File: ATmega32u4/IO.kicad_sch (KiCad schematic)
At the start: 14 parts, among them SW1 HWB, SW2 RESET

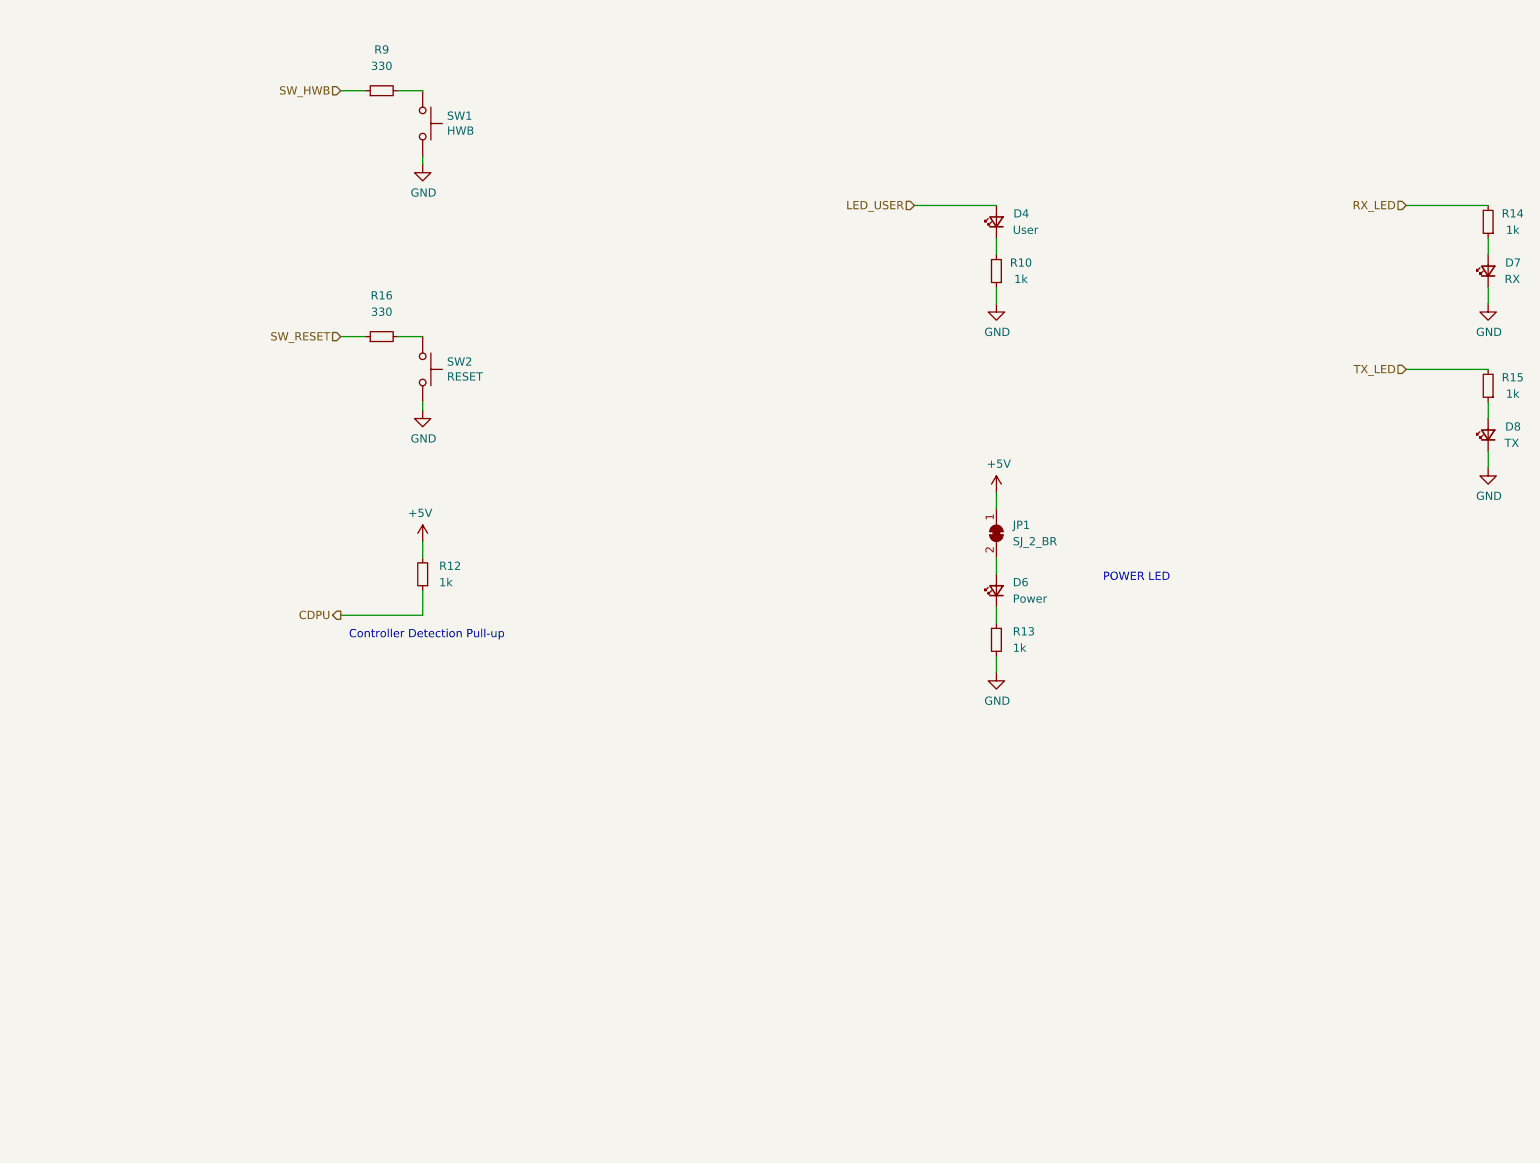
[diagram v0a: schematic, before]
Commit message: Schematic, routing and layout changes post review.
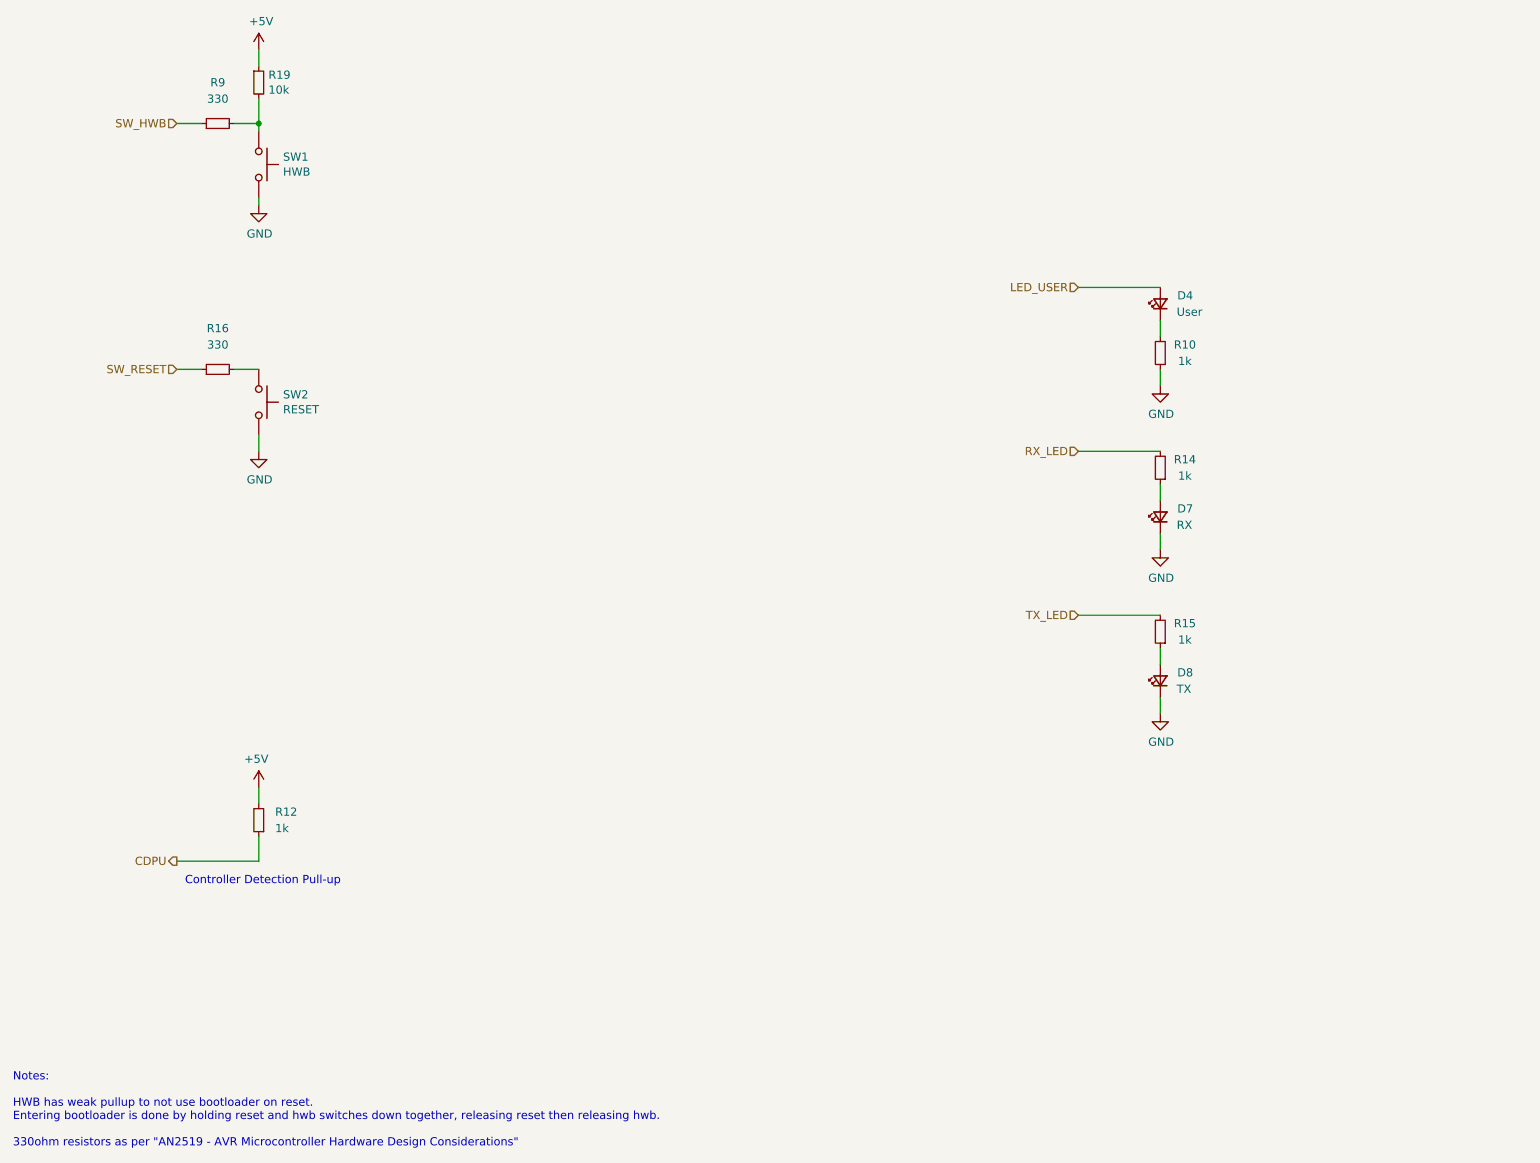
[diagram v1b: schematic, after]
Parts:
- removed D6: Power, LED_SMD:LED_0603_1608Metric, symbol Device:LED_Small
- removed JP1: SJ_2_BR, Jumper:SolderJumper-2_P1.3mm_Bridged_RoundedPad1.0x1.5mm, symbol Jumper:SolderJumper_2_Bridged
- removed R13: 1k, Resistor_SMD:R_0603_1608Metric, symbol Device:R_Small
- added R19: 10k, Resistor_SMD:R_0603_1608Metric, symbol Device:R_Small
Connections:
- net +5V: now also R19.1
- net at R9.2, SW1.1: now also R19.2
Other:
- note added: "Notes: HWB has weak pullup to not use bootloader on reset. Entering bootloader is done by holding reset and hwb switches down together, releasing reset then releasing hwb. 330ohm resistors as per "AN2519 - AVR Microcontroller Hardware Design Considerations""
- note removed: "POWER LED"
- moved on the sheet: D4, D7, D8, R10, R12, R14, R15, R16, R9, SW1, SW2

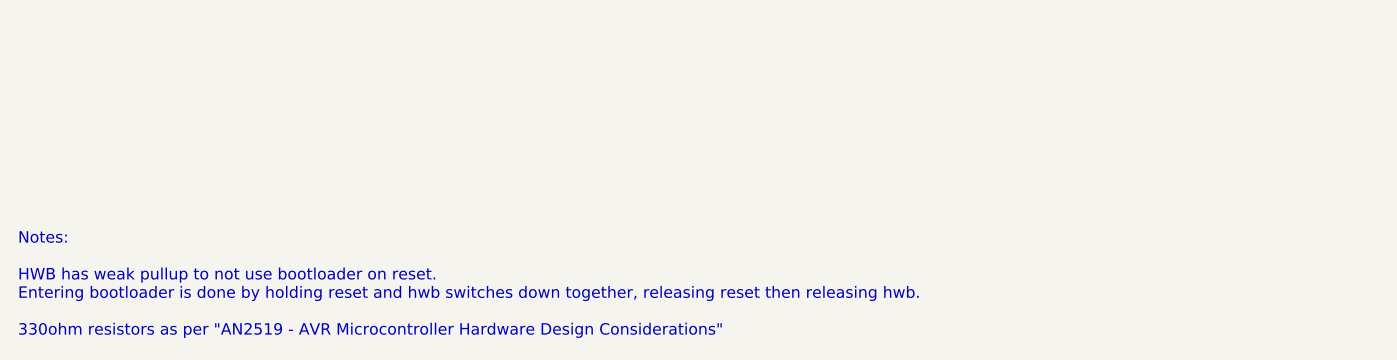
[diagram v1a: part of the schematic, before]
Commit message: Update notes, add io for reading cc pins, minor changes to schematic and routing.
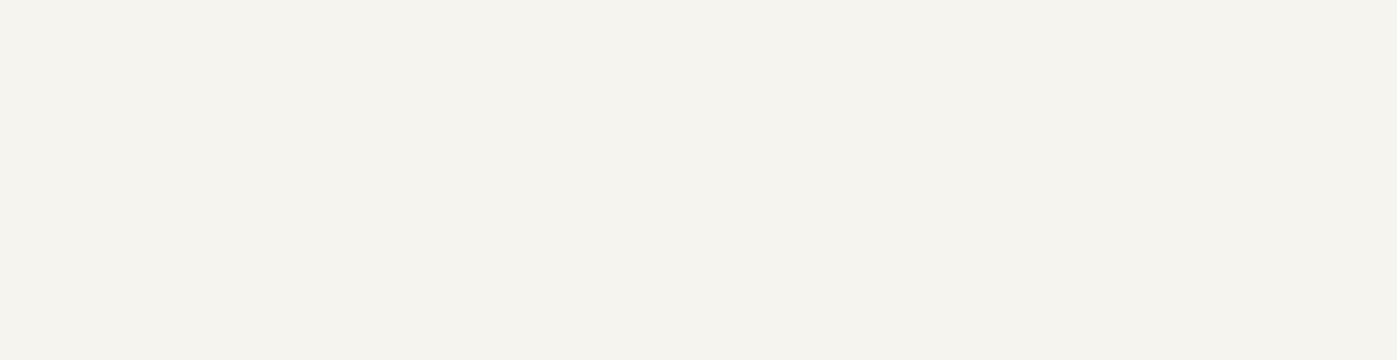
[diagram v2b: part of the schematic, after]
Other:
- note removed: "Notes: HWB has weak pullup to not use bootloader on reset. Entering bootloader is done by holding reset and hwb switches down together, releasing reset then releasing hwb. 330ohm resistors as per "AN2519 - AVR Microcontroller Hardware Design Considerations""
- title: (none) -> OpenRetroPad
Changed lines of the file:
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@@
 (kicad_sch (version 20211123) (generator eeschema)
   (paper "A4")
+  (title_block
+    (title "OpenRetroPad")
+    (date "2022-12-29")
+    (rev "2")
+    (comment 3 "github.com/OpenRetroPad")
+    (comment 4 "ATmega32u4")
+  )
   (junction (at 50.8 38.1) (diameter 0) (color 0 0 0 0)
   )
@@
     (effects (font (size 1.27 1.27)) (justify left bottom))
   )
-  (text "Notes:\n\nHWB has weak pullup to not use bootloader on reset.\nEntering bootloader is done by holding reset and hwb switches down together, releasing reset then releasing hwb.\n\n330ohm resistors as per \"AN2519 - AVR Microcontroller Hardware Design Considerations\""
-    (at 12.7 196.85 0)
-    (effects (font (size 1.27 1.27)) (justify left bottom))
-  )
